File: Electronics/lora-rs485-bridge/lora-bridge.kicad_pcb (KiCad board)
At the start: 4 copper layers, 63 x 50 mm, 73 parts, among them J1 battery, J2 ANT, J3 i2c, J4 rs485, J5 SWD, J9 USB micro, Q1 Q_PMOS_GSD, Q2 Q_NMOS_GSD, Q3 Q_PMOS_GSD, Q4 Q_PMOS_GSD, Q7 Q_PMOS_GSD, SW1 SW_Test, SW2 SW_Reset, U1 SN65HVD72, U2 ATSAMD21G18A-AUT, U3 RFM95W-868S2, U4 NCP718, Y1 32.768

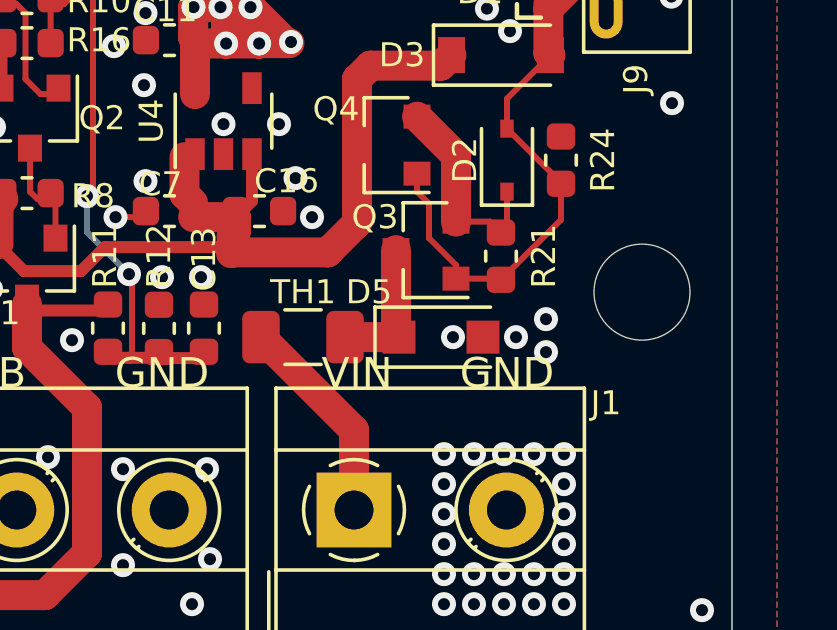
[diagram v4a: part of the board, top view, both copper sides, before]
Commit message: Fix info on silkscreen, remove RF connector pads from paste layer
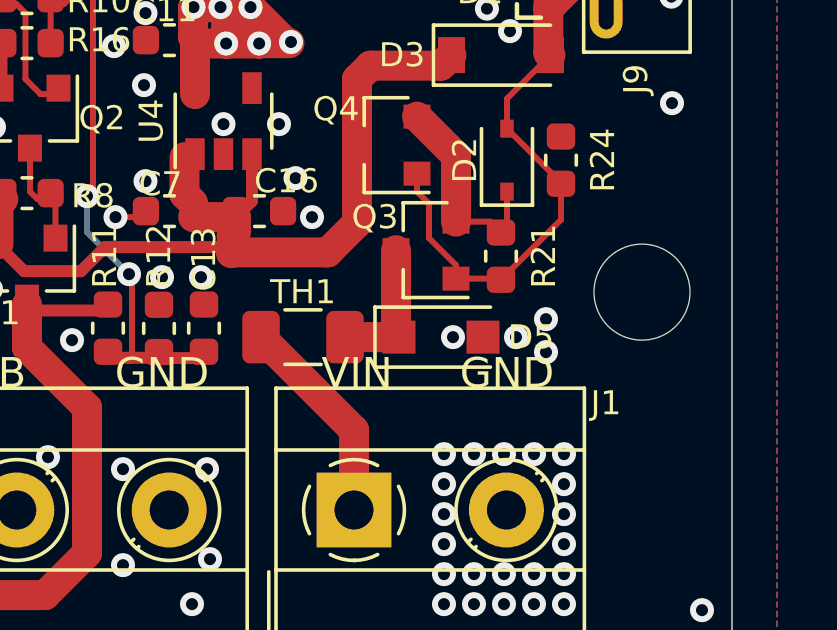
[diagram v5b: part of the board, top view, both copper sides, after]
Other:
- board text added: "Output current: 0.5A max"
- board text added: "https://github.com/RainDrop-lora/raindrop https://www.tindie.com/stores/miceuz/"
- board text removed: "Output current: 1A max"
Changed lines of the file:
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@@
   (general
     (thickness 1.6)
-    (drawings 27)
+    (drawings 28)
     (tracks 777)
     (modules 73)
@@
     (add_net "/ANTENNA")
   )
+  (module "miceuz-lib:SMA_6.35_EdgeMount" (layer "F.Cu")
+    (at 87.1 119.8 180)
+    (descr "http://www.amphenolrf.com/132289.html")
+    (tags "SMA")
+    (attr smd)
+    (fp_text reference "J2" (at -3.96 -3 270) (layer "F.SilkS")
+      (effects (font (size 1 1) (thickness 0.15)))
+    )
+    (fp_text value "ANT" (at 5 6 180) (layer "F.Fab")
+      (effects (font (size 1 1) (thickness 0.15)))
+    )
+    (fp_line (start -1.91 5.08) (end 4.445 5.08) (layer "F.Fab") (width 0.1))
+    (fp_line (start -1.91 3.81) (end -1.91 5.08) (layer "F.Fab") (width 0.1))
+    (fp_line (start 2.54 3.81) (end -1.91 3.81) (layer "F.Fab") (width 0.1))
+    (fp_line (start 2.54 -3.81) (end 2.54 3.81) (layer "F.Fab") (width 0.1))
+    (fp_line (start -1.91 -3.81) (end 2.54 -3.81) (layer "F.Fab") (width 0.1))
+    (fp_line (start -1.91 -5.08) (end -1.91 -3.81) (layer "F.Fab") (width 0.1))
+    (fp_line (start -1.91 -5.08) (end 4.445 -5.08) (layer "F.Fab") (width 0.1))
+    (fp_line (start 4.445 -3.81) (end 4.445 -5.08) (layer "F.Fab") (width 0.1))
+    (fp_line (start 4.445 5.08) (end 4.445 3.81) (layer "F.Fab") (width 0.1))
+    (fp_line (start 13.97 3.81) (end 4.445 3.81) (layer "F.Fab") (width 0.1))
+    (fp_line (start 13.97 -3.81) (end 13.97 3.81) (layer "F.Fab") (width 0.1))
+    (fp_line (start 4.445 -3.81) (end 13.97 -3.81) (layer "F.Fab") (width 0.1))
+    (fp_line (start -3.04 5.58) (end -3.04 -5.58) (layer "B.CrtYd") (width 0.05))
+    (fp_line (start 14.47 5.58) (end -3.04 5.58) (layer "B.CrtYd") (width 0.05))
+    (fp_line (start 14.47 -5.58) (end 14.47 5.58) (layer "B.CrtYd") (width 0.05))
+    (fp_line (start 14.47 -5.58) (end -3.04 -5.58) (layer "B.CrtYd") (width 0.05))
+    (fp_line (start -3.04 5.58) (end -3.04 -5.58) (layer "F.CrtYd") (width 0.05))
+    (fp_line (start 14.47 5.58) (end -3.04 5.58) (layer "F.CrtYd") (width 0.05))
+    (fp_line (start 14.47 -5.58) (end 14.47 5.58) (layer "F.CrtYd") (width 0.05))
+    (fp_line (start 14.47 -5.58) (end -3.04 -5.58) (layer "F.CrtYd") (width 0.05))
+    (fp_text user "%R" (at 4.79 0 90) (layer "F.Fab")
+      (effects (font (size 1 1) (thickness 0.15)))
+    )
+    (fp_line (start 2.54 -0.75) (end 3.54 0) (layer "F.Fab") (width 0.1))
+    (fp_line (start 3.54 0) (end 2.54 0.75) (layer "F.Fab") (width 0.1))
+    (fp_line (start -3.21 0) (end -3.71 -0.25) (layer "F.SilkS") (width 0.12))
+    (fp_line (start -3.71 -0.25) (end -3.71 0.25) (layer "F.SilkS") (width 0.12))
+    (fp_line (start -3.71 0.25) (end -3.21 0) (layer "F.SilkS") (width 0.12))
+    (pad "2" smd rect (at 0 2.825 270) (size 1.35 4.2) (layers "B.Cu" "B.Mask")
+      (net 1 "GND"))
+    (pad "2" smd rect (at 0 -2.825 270) (size 1.35 4.2) (layers "B.Cu" "B.Mask")
+      (net 1 "GND"))
+    (pad "2" smd rect (at 0 2.825 270) (size 1.35 4.2) (layers "F.Cu" "F.Mask")
+      (net 1 "GND"))
+    (pad "2" smd rect (at 0 -2.825 270) (size 1.35 4.2) (layers "F.Cu" "F.Mask")
+      (net 1 "GND"))
+    (pad "1" smd rect (at 0.15 0 270) (size 1.27 3.7) (layers "F.Cu" "F.Mask")
+      (net 49 "/ANTENNA"))
+    (model "${KIPRJMOD}/SMA-J-P-H-ST-EM1.STP--3DModel-STEP-66336.STEP"
+      (offset (xyz 4 0 0.55))
+      (scale (xyz 1 1 1))
+      (rotate (xyz 0 -90 90))
+    )
+  )
   (module "Diode_SMD:D_SOD-323" (layer "F.Cu")
     (at 140.5 126.9 90)
@@
     )
   )
-  (module "miceuz-lib:SMA_6.35_EdgeMount" (layer "F.Cu")
-    (at 87.1 119.8 180)
-    (descr "http://www.amphenolrf.com/132289.html")
-    (tags "SMA")
-    (attr smd)
-    (fp_text reference "J2" (at -3.96 -3 90) (layer "F.SilkS")
-      (effects (font (size 1 1) (thickness 0.15)))
-    )
-    (fp_text value "ANT" (at 5 6) (layer "F.Fab")
-      (effects (font (size 1 1) (thickness 0.15)))
-    )
-    (fp_line (start -1.91 5.08) (end 4.445 5.08) (layer "F.Fab") (width 0.1))
-    (fp_line (start -1.91 3.81) (end -1.91 5.08) (layer "F.Fab") (width 0.1))
-    (fp_line (start 2.54 3.81) (end -1.91 3.81) (layer "F.Fab") (width 0.1))
-    (fp_line (start 2.54 -3.81) (end 2.54 3.81) (layer "F.Fab") (width 0.1))
-    (fp_line (start -1.91 -3.81) (end 2.54 -3.81) (layer "F.Fab") (width 0.1))
-    (fp_line (start -1.91 -5.08) (end -1.91 -3.81) (layer "F.Fab") (width 0.1))
-    (fp_line (start -1.91 -5.08) (end 4.445 -5.08) (layer "F.Fab") (width 0.1))
-    (fp_line (start 4.445 -3.81) (end 4.445 -5.08) (layer "F.Fab") (width 0.1))
-    (fp_line (start 4.445 5.08) (end 4.445 3.81) (layer "F.Fab") (width 0.1))
-    (fp_line (start 13.97 3.81) (end 4.445 3.81) (layer "F.Fab") (width 0.1))
-    (fp_line (start 13.97 -3.81) (end 13.97 3.81) (layer "F.Fab") (width 0.1))
-    (fp_line (start 4.445 -3.81) (end 13.97 -3.81) (layer "F.Fab") (width 0.1))
-    (fp_line (start -3.04 5.58) (end -3.04 -5.58) (layer "B.CrtYd") (width 0.05))
-    (fp_line (start 14.47 5.58) (end -3.04 5.58) (layer "B.CrtYd") (width 0.05))
-    (fp_line (start 14.47 -5.58) (end 14.47 5.58) (layer "B.CrtYd") (width 0.05))
-    (fp_line (start 14.47 -5.58) (end -3.04 -5.58) (layer "B.CrtYd") (width 0.05))
-    (fp_line (start -3.04 5.58) (end -3.04 -5.58) (layer "F.CrtYd") (width 0.05))
-    (fp_line (start 14.47 5.58) (end -3.04 5.58) (layer "F.CrtYd") (width 0.05))
-    (fp_line (start 14.47 -5.58) (end 14.47 5.58) (layer "F.CrtYd") (width 0.05))
-    (fp_line (start 14.47 -5.58) (end -3.04 -5.58) (layer "F.CrtYd") (width 0.05))
-    (fp_text user "%R" (at 4.79 0 270) (layer "F.Fab")
-      (effects (font (size 1 1) (thickness 0.15)))
-    )
-    (fp_line (start 2.54 -0.75) (end 3.54 0) (layer "F.Fab") (width 0.1))
-    (fp_line (start 3.54 0) (end 2.54 0.75) (layer "F.Fab") (width 0.1))
-    (fp_line (start -3.21 0) (end -3.71 -0.25) (layer "F.SilkS") (width 0.12))
-    (fp_line (start -3.71 -0.25) (end -3.71 0.25) (layer "F.SilkS") (width 0.12))
-    (fp_line (start -3.71 0.25) (end -3.21 0) (layer "F.SilkS") (width 0.12))
-    (pad "2" smd rect (at 0 2.825 270) (size 1.35 4.2) (layers "B.Cu" "B.Paste" "B.Mask")
-      (net 1 "GND"))
-    (pad "2" smd rect (at 0 -2.825 270) (size 1.35 4.2) (layers "B.Cu" "B.Paste" "B.Mask")
-      (net 1 "GND"))
-    (pad "2" smd rect (at 0 2.825 270) (size 1.35 4.2) (layers "F.Cu" "F.Paste" "F.Mask")
-      (net 1 "GND"))
-    (pad "2" smd rect (at 0 -2.825 270) (size 1.35 4.2) (layers "F.Cu" "F.Paste" "F.Mask")
-      (net 1 "GND"))
-    (pad "1" smd rect (at 0.15 0 270) (size 1.27 3.7) (layers "F.Cu" "F.Paste" "F.Mask")
-      (net 49 "/ANTENNA"))
-    (model "${KIPRJMOD}/SMA-J-P-H-ST-EM1.STP--3DModel-STEP-66336.STEP"
-      (offset (xyz 4 0 0.55))
-      (scale (xyz 1 1 1))
-      (rotate (xyz 0 -90 90))
-    )
-  )
   (module "Resistor_SMD:R_0603_1608Metric" (layer "F.Cu")
     (at 139.7 107.4 180)
@@
     (tags "D_SOD-123F")
     (attr smd)
-    (fp_text reference "D5" (at -2.4 -1.5) (layer "F.SilkS")
+    (fp_text reference "D5" (at 3 0) (layer "F.SilkS")
       (effects (font (size 0.8 0.8) (thickness 0.15)))
     )
@@
     )
   )
+  (gr_text "https://github.com/RainDrop-lora/raindrop\nhttps://www.tindie.com/stores/miceuz/" (at 116.6 96.3 180) (layer "B.SilkS")
+    (effects (font (size 1 1) (thickness 0.15)) (justify mirror))
+  )
   (gr_text "Manufacturer:\nAlbertas Mickėnas\nMindaugo 25\n03011 Vilnius\nLithuania" (at 147 104.2 180) (layer "B.SilkS")
     (effects (font (size 1 1) (thickness 0.15)) (justify right mirror))
@@
     (effects (font (size 1 1) (thickness 0.15)) (justify mirror))
   )
-  (gr_text "\nOutput current:\n1A max" (at 119.7 135.6 180) (layer "B.SilkS")
+  (gr_text "Output current:\n0.5A max" (at 119.7 135.6 180) (layer "B.SilkS")
     (effects (font (size 1 1) (thickness 0.15)) (justify mirror))
   )

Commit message: Move R11 and accompanying components a bit so it's easier to replace it. Add fiducials. Generate gerbers for v1.2
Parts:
- removed the REF*** at (142.8, 112.1)
- added FID1: Fiducial, Fiducials:Fiducial_1mm_Dia_2mm_Outer, F.Cu at (146.8, 98.0)
- added FID2: Fiducial, Fiducials:Fiducial_1mm_Dia_2mm_Outer, F.Cu at (86.2, 140.2)
- R11: value 10k -> 20k
- R13, R14, R15: value 10k -> 1k
- R17, R19, R24: value 150 -> 1M
- R3, R9: value 10k -> 1M
- moved REF*** 9.80 mm to (142.9, 112.0)
- moved R12 0.56 mm to (129.1, 132.0), turned to 90 degrees
- moved C13 0.54 mm to (130.6, 132.0), turned to -90 degrees
- moved R11 0.51 mm to (127.3, 132.0), turned to 90 degrees
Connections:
- J3 pad 1: /VOUT -> /VOUT_1
- J4 pad 1: /VOUT_1 -> /VOUT
- Q1 pad 3: /VOUT_1 -> /VOUT
- Q7 pad 3: /VOUT -> /VOUT_1
- R11 pad 1: /VOUT_1 -> /VOUT
- R6 pad 1: /VOUT -> /VOUT_1
- R7 pad 1: /VOUT -> /VOUT_1
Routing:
- net /VOUT_1: track 26.1 -> 20.4 mm
- net /VOUT: track 20.4 -> 25.8 mm
- net /BATT_MON: track 31.5 -> 29.4 mm
- net GND: vias 218 -> 226
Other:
- board text added: "LORA-RS485 bridge v1.2 2020-01-24"
- board text removed: "LORA-RS485 bridge v1.2 2020-01-16"

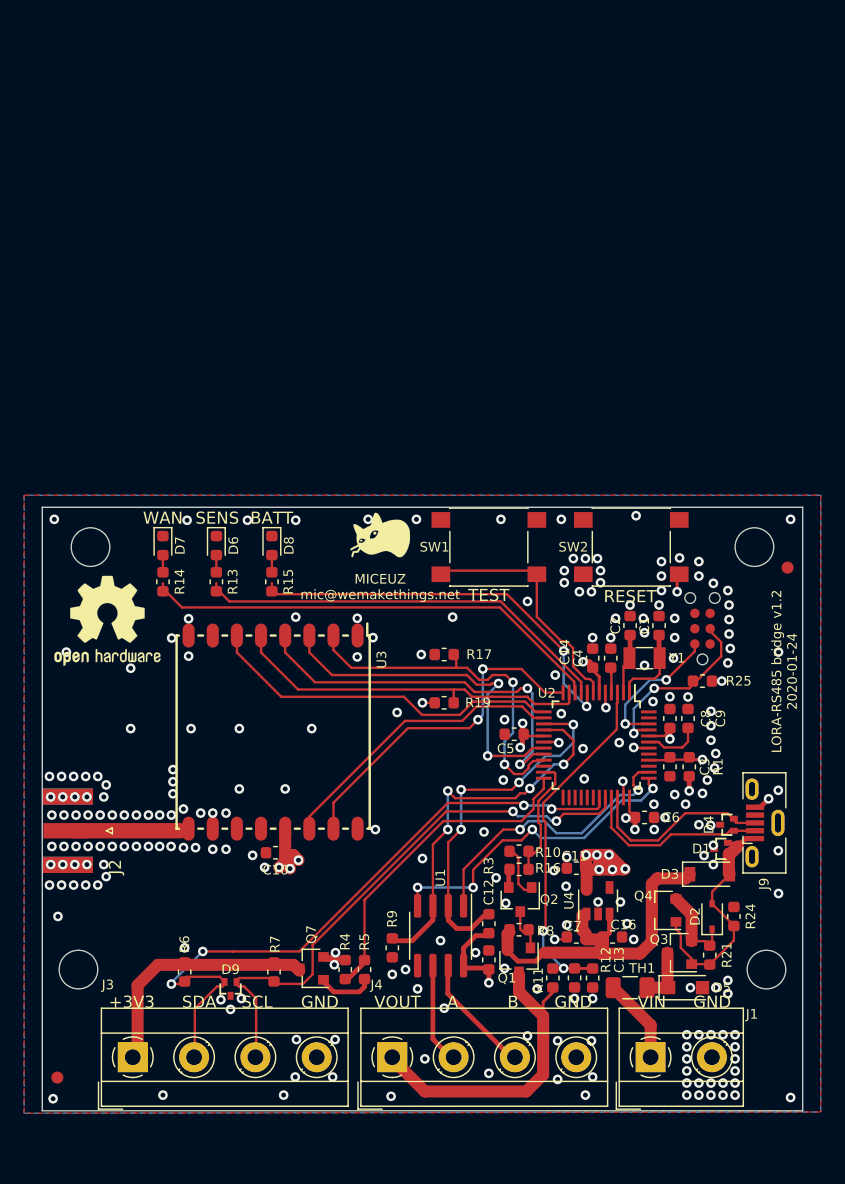
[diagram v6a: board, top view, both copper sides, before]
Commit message: Move around vias so power planes are not so much broken. Move connectors closer together so all of them are on 5.08mm grid
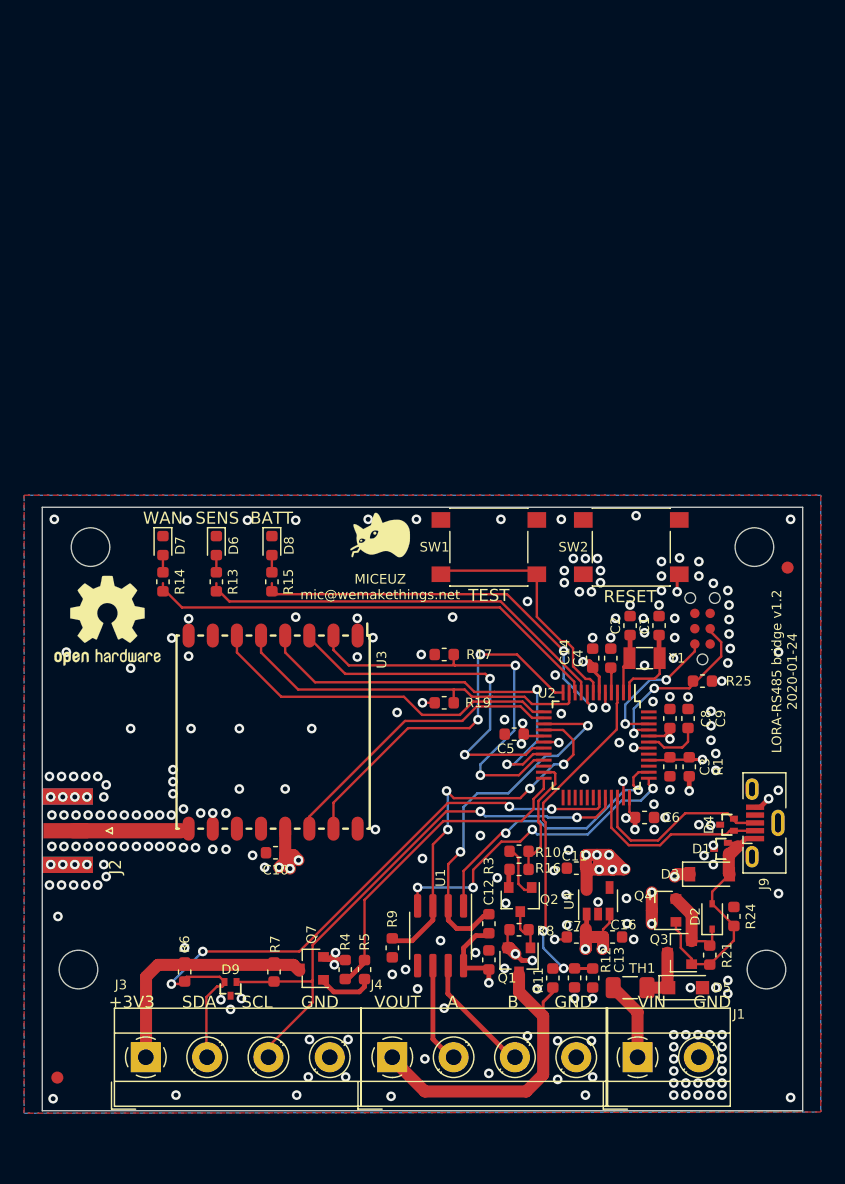
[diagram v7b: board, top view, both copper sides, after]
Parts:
- moved J1 1.08 mm to (134.3, 138.6)
- moved J3 1.08 mm to (93.6, 138.6)
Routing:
- net +BATT: track 31.8 -> 15.5 mm, vias 0 -> 7
- net /RFM_MISO: track 30.0 -> 34.1 mm
- net /RFM_SCK: track 32.0 -> 34.5 mm
- net /DIO01: track 29.0 -> 30.8 mm
- net /RFM_MOSI: track 29.3 -> 30.3 mm
- net /LED3: track 33.3 -> 33.9 mm
- net /~RS485_RE: track 30.2 -> 30.8 mm, vias 4 -> 2
- net /I2C_SDA: track 55.7 -> 55.2 mm
- net GND: vias 226 -> 221
- added copper zone on In2.Cu, net +BATT
